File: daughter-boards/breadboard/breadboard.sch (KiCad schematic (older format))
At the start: 53 parts, among them P1 SAMTEC-QSE-020-01-F-D-A, P2 SAMTEC-QSE-020-01-F-D-A

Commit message: Updated daughterboards for the new Scaffold socket
Update breadboard, smartcard and STM32F205 daughterboards to fit the
new socket format of Scaffold v1.1 hardware.
Previous socket format is now deprecated.
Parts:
- removed P1, P2: SAMTEC-QSE-020-01-F-D-A, mykicadlibs:SAMTEC-QSE-020-01-F-D-A, symbol mylib:SAMTEC-QSE-020-01-F-D-A
- added J1, J2: Conn_02x10_Odd_Even, Connector_PinSocket_2.54mm:PinSocket_2x10_P2.54mm_Vertical, symbol Connector_Generic:Conn_02x10_Odd_Even
- added LOGO1: DUNGEON_LOGO, mykicadlibs:donjon-3000, symbol mylib:DUNGEON_LOGO
- added TP100, TP101, TP102, TP103, TP104, TP105, TP106, TP107, TP108, TP109, TP110, TP111, TP112, TP113, TP114, TP115, TP116, TP117, TP118, TP119, TP120, TP121, TP122, TP123, TP124, TP125, TP126, TP127, TP128, TP129, TP130, TP131, TP132, TP133, TP134, TP135, TP136, TP137, TP138, TP139, TP140, TP141, TP142, TP143, TP144, TP145, TP146, TP147, TP148, TP149, TP150, TP151, TP152, TP153, TP154, TP155, TP156, TP157, TP158, TP159, TP160, TP161, TP162, TP163, TP164, TP165, TP166, TP167, TP168, TP169, TP170, TP171, TP172, TP173, TP174, TP175, TP176, TP177, TP178, TP179, TP180, TP181, TP182, TP183, TP184, TP185, TP186, TP187, TP188, TP189, TP190, TP191, TP192, TP193, TP194, TP195, TP196, TP197, TP198, TP199, TP200, TP201, TP202, TP203, TP204, TP205, TP206, TP207, TP208, TP209, TP210, TP211, TP212, TP213, TP214, TP215, TP216, TP217, TP218, TP219, TP220, TP221, TP222, TP223, TP224, TP225, TP226, TP227, TP228, TP229, TP230, TP231, TP232, TP233, TP234, TP235, TP236, TP237, TP238, TP239, TP240, TP241, TP242, TP243, TP244, TP245, TP246, TP247, TP248, TP249, TP250, TP251, TP252, TP253, TP254, TP255, TP256, TP257, TP258, TP259, TP260, TP261, TP262, TP263, TP264, TP265, TP266, TP267, TP268, TP269, TP270, TP271, TP272, TP273, TP274, TP275, TP276, TP277, TP278, TP279, TP280, TP281, TP282, TP283, TP284, TP285, TP286, TP287, TP288, TP289, TP290, TP291, TP292, TP293, TP294, TP295, TP296, TP297, TP298, TP299, TP300, TP301, TP302, TP303, TP304, TP305, TP306, TP307, TP308, TP309, TP310, TP311, TP312, TP313, TP314, TP315, TP316, TP317, TP318, TP319, TP320, TP321, TP322, TP323, TP324, TP325, TP326, TP327, TP328, TP52, TP53, TP54, TP55, TP56, TP57, TP58, TP59, TP60, TP61, TP62, TP63, TP64, TP65, TP66, TP67, TP68, TP69, TP70, TP71, TP72, TP73, TP74, TP75, TP76, TP77, TP78, TP79, TP80, TP81, TP82, TP83, TP84, TP85, TP86, TP87, TP88, TP89, TP90, TP91, TP92, TP93, TP94, TP95, TP96, TP97, TP98, TP99: TestPoint, mykicadlibs:TEST_BREADBOARD_RECTANGULAR, symbol Connector:TestPoint
- TP1, TP10, TP11, TP12, TP13, TP14, TP15, TP16, TP17, TP18, TP19, TP2, TP20, TP21, TP22, TP23, TP24, TP25, TP26, TP27, TP28, TP29, TP3, TP30, TP31, TP32, TP33, TP34, TP35, TP36, TP37, TP38, TP39, TP4, TP40, TP41, TP42, TP43, TP44, TP45, TP46, TP47, TP48, TP49, TP5, TP50, TP51, TP6, TP7, TP8, TP9: footprint TestPoint:TestPoint_Pad_D1.5mm -> mykicadlibs:TEST_BREADBOARD_RECTANGULAR
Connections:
- net labels added: D0, D1, D10, D11, D12, D13, D14, D15, D2, D3, D4, D5, D6, D7, D8, D9, VDD, VDDA
- net labels removed: +3V3
- wire segments 156 -> 98
- no-connect marks 0 -> 260
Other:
- note removed: "Scaffold GND,\ndon't connect to DUT"

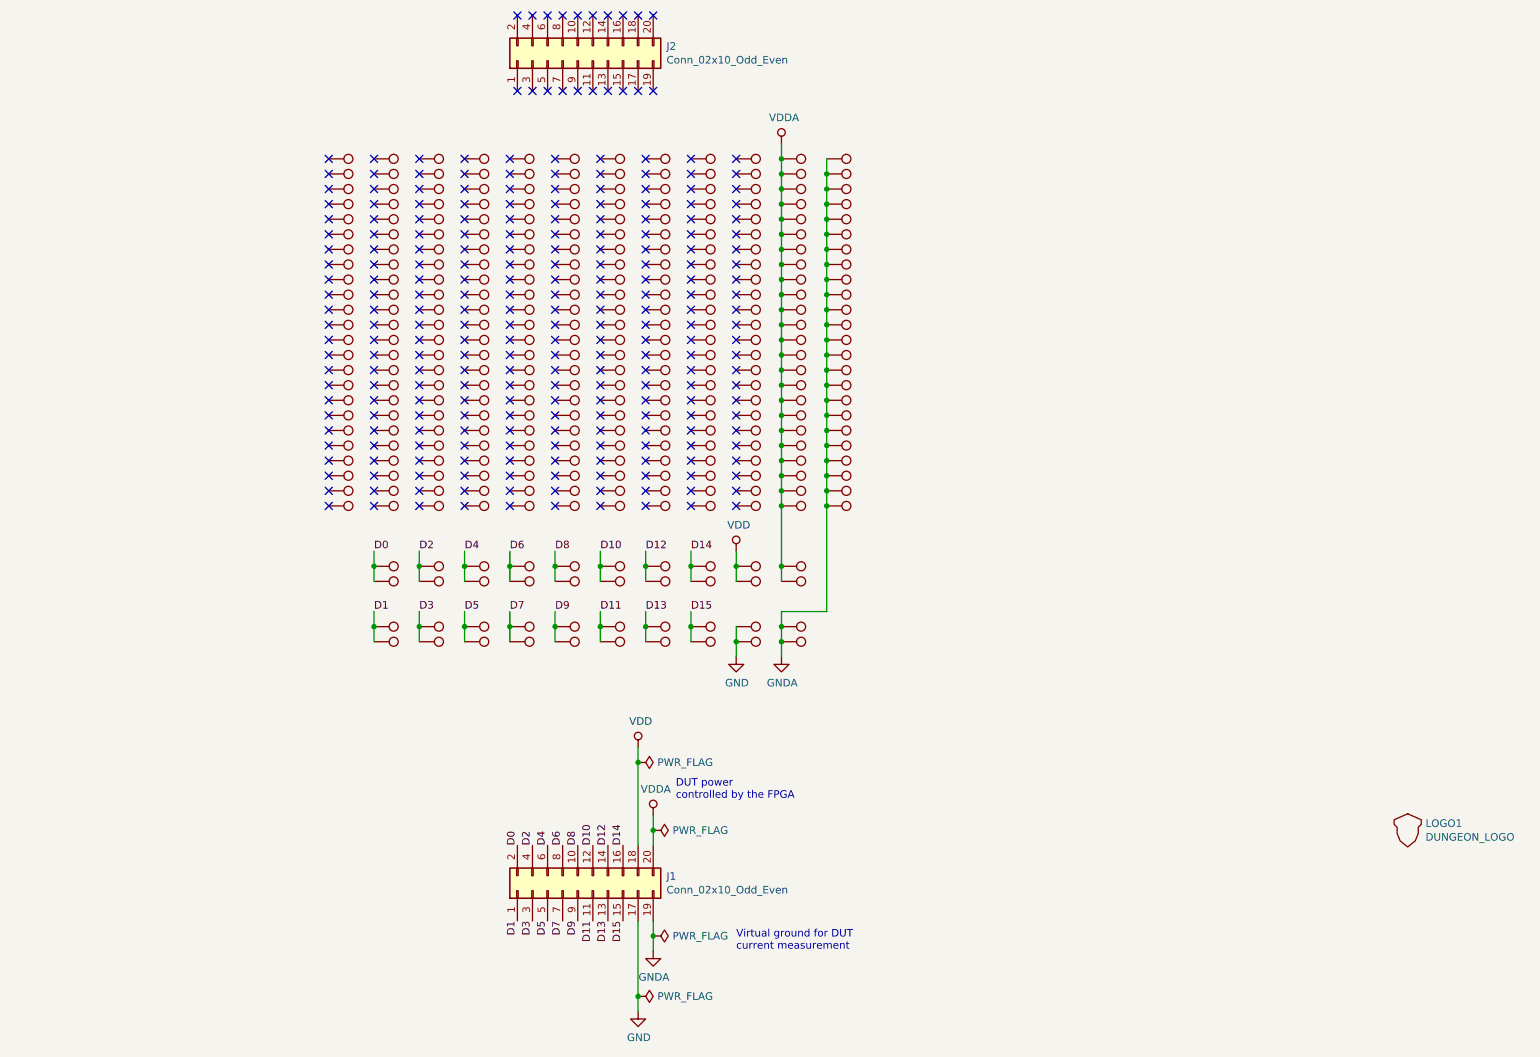
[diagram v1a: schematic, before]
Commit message: Fixed holes in breadboard daughterboard.
Replaced plated holes with non-plated holes for easier solderability.
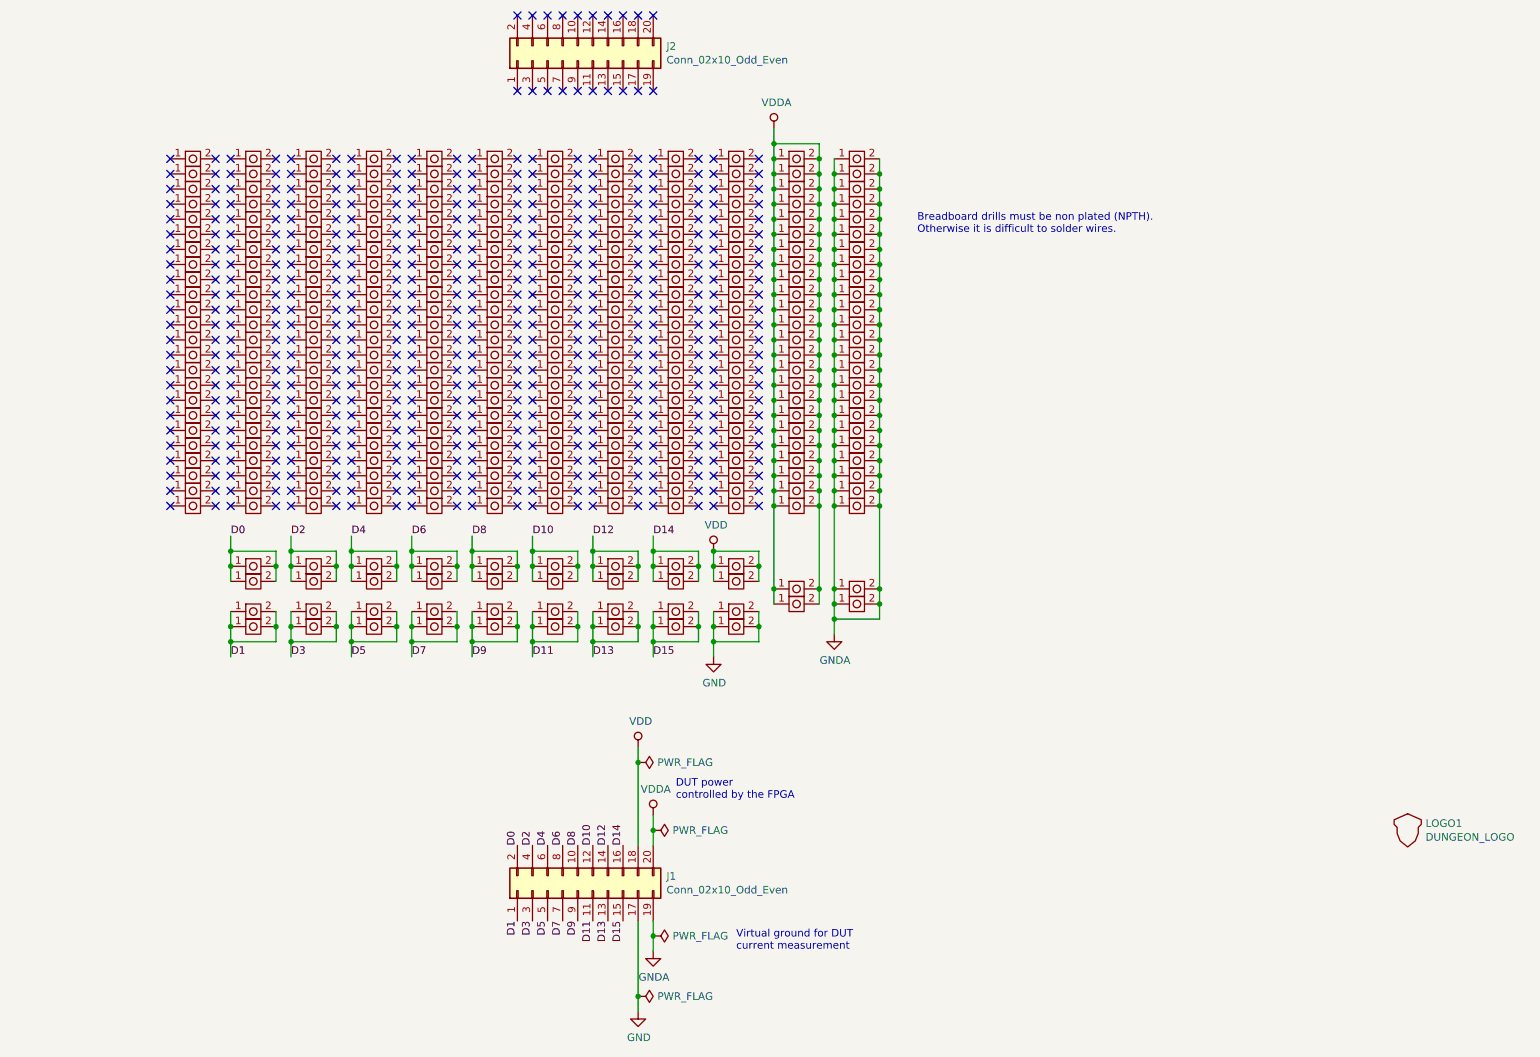
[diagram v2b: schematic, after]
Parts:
- removed TP1, TP10, TP100, TP101, TP102, TP103, TP104, TP105, TP106, TP107, TP108, TP109, TP11, TP110, TP111, TP112, TP113, TP114, TP115, TP116, TP117, TP118, TP119, TP12, TP120, TP121, TP122, TP123, TP124, TP125, TP126, TP127, TP128, TP129, TP13, TP130, TP131, TP132, TP133, TP134, TP135, TP136, TP137, TP138, TP139, TP14, TP140, TP141, TP142, TP143, TP144, TP145, TP146, TP147, TP148, TP149, TP15, TP150, TP151, TP152, TP153, TP154, TP155, TP156, TP157, TP158, TP159, TP16, TP160, TP161, TP162, TP163, TP164, TP165, TP166, TP167, TP168, TP169, TP17, TP170, TP171, TP172, TP173, TP174, TP175, TP176, TP177, TP178, TP179, TP18, TP180, TP181, TP182, TP183, TP184, TP185, TP186, TP187, TP188, TP189, TP19, TP190, TP191, TP192, TP193, TP194, TP195, TP196, TP197, TP198, TP199, TP2, TP20, TP200, TP201, TP202, TP203, TP204, TP205, TP206, TP207, TP208, TP209, TP21, TP210, TP211, TP212, TP213, TP214, TP215, TP216, TP217, TP218, TP219, TP22, TP220, TP221, TP222, TP223, TP224, TP225, TP226, TP227, TP228, TP229, TP23, TP230, TP231, TP232, TP233, TP234, TP235, TP236, TP237, TP238, TP239, TP24, TP240, TP241, TP242, TP243, TP244, TP245, TP246, TP247, TP248, TP249, TP25, TP250, TP251, TP252, TP253, TP254, TP255, TP256, TP257, TP258, TP259, TP26, TP260, TP261, TP262, TP263, TP264, TP265, TP266, TP267, TP268, TP269, TP27, TP270, TP271, TP272, TP273, TP274, TP275, TP276, TP277, TP278, TP279, TP28, TP280, TP281, TP282, TP283, TP284, TP285, TP286, TP287, TP288, TP289, TP29, TP290, TP291, TP292, TP293, TP294, TP295, TP296, TP297, TP298, TP299, TP3, TP30, TP300, TP301, TP302, TP303, TP304, TP305, TP306, TP307, TP308, TP309, TP31, TP310, TP311, TP312, TP313, TP314, TP315, TP316, TP317, TP318, TP319, TP32, TP320, TP321, TP322, TP323, TP324, TP325, TP326, TP327, TP328, TP33, TP34, TP35, TP36, TP37, TP38, TP39, TP4, TP40, TP41, TP42, TP43, TP44, TP45, TP46, TP47, TP48, TP49, TP5, TP50, TP51, TP52, TP53, TP54, TP55, TP56, TP57, TP58, TP59, TP6, TP60, TP61, TP62, TP63, TP64, TP65, TP66, TP67, TP68, TP69, TP7, TP70, TP71, TP72, TP73, TP74, TP75, TP76, TP77, TP78, TP79, TP8, TP80, TP81, TP82, TP83, TP84, TP85, TP86, TP87, TP88, TP89, TP9, TP90, TP91, TP92, TP93, TP94, TP95, TP96, TP97, TP98, TP99: TestPoint, mykicadlibs:TEST_BREADBOARD_RECTANGULAR, symbol Connector:TestPoint
- added U1, U10, U100, U101, U102, U103, U104, U105, U106, U107, U108, U109, U11, U110, U111, U112, U113, U114, U115, U116, U117, U118, U119, U12, U120, U121, U122, U123, U124, U125, U126, U127, U128, U129, U13, U130, U131, U132, U133, U134, U135, U136, U137, U138, U139, U14, U140, U141, U142, U143, U144, U145, U146, U147, U148, U149, U15, U150, U151, U152, U153, U154, U155, U156, U157, U158, U159, U16, U160, U161, U162, U163, U164, U165, U166, U167, U168, U169, U17, U170, U171, U172, U173, U174, U175, U176, U177, U178, U179, U18, U180, U181, U182, U183, U184, U185, U186, U187, U188, U189, U19, U190, U191, U192, U193, U194, U195, U196, U197, U198, U199, U2, U20, U200, U201, U202, U203, U204, U205, U206, U207, U208, U209, U21, U210, U211, U212, U213, U214, U215, U216, U217, U218, U219, U22, U220, U221, U222, U223, U224, U225, U226, U227, U228, U229, U23, U230, U231, U232, U233, U234, U235, U236, U237, U238, U239, U24, U240, U241, U242, U243, U244, U245, U246, U247, U248, U249, U25, U250, U251, U252, U253, U254, U255, U256, U257, U258, U259, U26, U260, U261, U262, U263, U264, U265, U266, U267, U268, U269, U27, U270, U271, U272, U273, U274, U275, U276, U277, U278, U279, U28, U280, U281, U282, U283, U284, U285, U286, U287, U288, U289, U29, U290, U291, U292, U293, U294, U295, U296, U297, U298, U299, U3, U30, U300, U301, U302, U303, U304, U305, U306, U307, U308, U309, U31, U310, U311, U312, U313, U314, U315, U316, U317, U318, U319, U32, U320, U321, U322, U323, U324, U325, U326, U327, U328, U33, U34, U35, U36, U37, U38, U39, U4, U40, U41, U42, U43, U44, U45, U46, U47, U48, U49, U5, U50, U51, U52, U53, U54, U55, U56, U57, U58, U59, U6, U60, U61, U62, U63, U64, U65, U66, U67, U68, U69, U7, U70, U71, U72, U73, U74, U75, U76, U77, U78, U79, U8, U80, U81, U82, U83, U84, U85, U86, U87, U88, U89, U9, U90, U91, U92, U93, U94, U95, U96, U97, U98, U99: BREADBOARD_NPTH, mykicadlibs:TEST_BREADBOARD_RECTANGULAR_NPTH2, symbol mylib:BREADBOARD_NPTH
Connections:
- net D0: now also U297.1, U297.2, U298.1, U298.2
- net D1: now also U299.1, U299.2, U300.1, U300.2
- net D10: now also U317.1, U317.2, U318.1, U318.2
- net D11: now also U319.1, U319.2, U320.1, U320.2
- net D12: now also U321.1, U321.2, U322.1, U322.2
- net D13: now also U323.1, U323.2, U324.1, U324.2
- net D14: now also U325.1, U325.2, U326.1, U326.2
- net D15: now also U327.1, U327.2, U328.1, U328.2
- net D2: now also U301.1, U301.2, U302.1, U302.2
- net D3: now also U303.1, U303.2, U304.1, U304.2
- net D4: now also U305.1, U305.2, U306.1, U306.2
- net D5: now also U307.1, U307.2, U308.1, U308.2
- net D6: now also U309.1, U309.2, U310.1, U310.2
- net D7: now also U311.1, U311.2, U312.1, U312.2
- net D8: now also U313.1, U313.2, U314.1, U314.2
- net D9: now also U315.1, U315.2, U316.1, U316.2
- net GND: now also U295.1, U295.2, U296.1, U296.2
- net GNDA: now also U267.1, U267.2, U268.1, U268.2, U269.1, U269.2, U270.1, U270.2, U271.1, U271.2, U272.1, U272.2, U273.1, U273.2, U274.1, U274.2, U275.1, U275.2, U276.1, U276.2, U277.1, U277.2, U278.1, U278.2, U279.1, U279.2, U280.1, U280.2, U281.1, U281.2, U282.1, U282.2, U283.1, U283.2, U284.1, U284.2, U285.1, U285.2, U286.1, U286.2, U287.1, U287.2, U288.1, U288.2, U289.1, U289.2, U290.1, U290.2, U291.1, U291.2, U292.1, U292.2
- net VDD: now also U293.1, U293.2, U294.1, U294.2
- net VDDA: now also U241.1, U241.2, U242.1, U242.2, U243.1, U243.2, U244.1, U244.2, U245.1, U245.2, U246.1, U246.2, U247.1, U247.2, U248.1, U248.2, U249.1, U249.2, U250.1, U250.2, U251.1, U251.2, U252.1, U252.2, U253.1, U253.2, U254.1, U254.2, U255.1, U255.2, U256.1, U256.2, U257.1, U257.2, U258.1, U258.2, U259.1, U259.2, U260.1, U260.2, U261.1, U261.2, U262.1, U262.2, U263.1, U263.2, U264.1, U264.2, U265.1, U265.2, U266.1, U266.2
- no-connect marks 260 -> 500
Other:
- note added: "Breadboard drills must be non plated (NPTH).\nOtherwise it is difficult to solder wires."
